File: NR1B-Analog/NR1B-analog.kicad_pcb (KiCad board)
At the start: 4 copper layers, 71.1 x 134.5 mm, 87 parts, among them J1 Conn_02x04_Odd_Even, J2 Conn_02x04_Odd_Even, J3 SWD, J8 UART, SW1 1-1571636-0, U1 DAC11001BPFBR, U10 LT3042MPMSE-PBF, U11 LDK320ADU120R, U12 20K, U13 OPA2189IDR, U14 DAC11001BPFBR, U2 ADR444ARZ, U3 OPA189IDGKT, U4 OPA2189IDR, U5 Pico, U6 OPA2189IDR, U7 LT3093EMSE-PBF, U8 20K, U9 10K, X1 NUCLEO144-ZIO

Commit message: BOM, fiducials
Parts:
- added FID1: Fiducial, Fiducial:Fiducial_0.5mm_Mask1.5mm, F.Cu at (50.8, 20.4)
- added FID2: Fiducial, Fiducial:Fiducial_0.5mm_Mask1.5mm, F.Cu at (118.1, 20.4)
- added FID3: Fiducial, Fiducial:Fiducial_0.5mm_Mask1.5mm, F.Cu at (117.1, 151.1)
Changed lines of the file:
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@@
       (net 70 "unconnected-(U8-Pad3)") (pinfunction "CW") (pintype "input+no_connect"))
+  )
+  (footprint "Fiducial:Fiducial_0.5mm_Mask1.5mm" (layer "F.Cu")
+    (at 50.77 20.35)
+    (descr "Circular Fiducial, 0.5mm bare copper, 1.5mm soldermask opening")
+    (tags "fiducial")
+    (property "Sheetfile" "NR1B-analog.kicad_sch")
+    (property "Sheetname" "")
+    (attr smd)
+    (fp_text reference "FID1" (at 2.73 -0.14) (layer "F.SilkS")
+      (effects (font (size 1 1) (thickness 0.15)))
+    )
+    (fp_text value "Fiducial" (at 0 1.7145) (layer "F.Fab")
+      (effects (font (size 1 1) (thickness 0.15)))
+    )
+    (fp_text user "${REFERENCE}" (at 0 0) (layer "F.Fab")
+      (effects (font (size 0.2 0.2) (thickness 0.04)))
+    )
+    (fp_circle (center 0 0) (end 1 0) (layer "F.CrtYd") (width 0.05) (fill none))
+    (fp_circle (center 0 0) (end 0.75 0) (layer "F.Fab") (width 0.1) (fill none))
+    (pad "" smd circle (at 0 0) (size 0.5 0.5) (layers "F.Cu" "F.Mask")
+      (solder_mask_margin 0.5) (clearance 0.5))
   )
   (footprint "Resistor_SMD:R_0603_1608Metric" (layer "F.Cu")
@@
     )
   )
+  (footprint "Fiducial:Fiducial_0.5mm_Mask1.5mm" (layer "F.Cu")
+    (at 117.1 151.11)
+    (descr "Circular Fiducial, 0.5mm bare copper, 1.5mm soldermask opening")
+    (tags "fiducial")
+    (property "Sheetfile" "NR1B-analog.kicad_sch")
+    (property "Sheetname" "")
+    (attr smd)
+    (fp_text reference "FID3" (at 0 -1.7145) (layer "F.SilkS")
+      (effects (font (size 1 1) (thickness 0.15)))
+    )
+    (fp_text value "Fiducial" (at 0 1.7145) (layer "F.Fab")
+      (effects (font (size 1 1) (thickness 0.15)))
+    )
+    (fp_text user "${REFERENCE}" (at 0 0) (layer "F.Fab")
+      (effects (font (size 0.2 0.2) (thickness 0.04)))
+    )
+    (fp_circle (center 0 0) (end 1 0) (layer "F.CrtYd") (width 0.05) (fill none))
+    (fp_circle (center 0 0) (end 0.75 0) (layer "F.Fab") (width 0.1) (fill none))
+    (pad "" smd circle (at 0 0) (size 0.5 0.5) (layers "F.Cu" "F.Mask")
+      (solder_mask_margin 0.5) (clearance 0.5))
+  )
   (footprint "Resistor_SMD:R_0603_1608Metric" (layer "F.Cu")
     (at 90.73 51.32 -90)
@@
     )
   )
+  (footprint "Fiducial:Fiducial_0.5mm_Mask1.5mm" (layer "F.Cu")
+    (at 118.08 20.35)
+    (descr "Circular Fiducial, 0.5mm bare copper, 1.5mm soldermask opening")
+    (tags "fiducial")
+    (property "Sheetfile" "NR1B-analog.kicad_sch")
+    (property "Sheetname" "")
+    (attr smd)
+    (fp_text reference "FID2" (at -2.98 0.12) (layer "F.SilkS")
+      (effects (font (size 1 1) (thickness 0.15)))
+    )
+    (fp_text value "Fiducial" (at 0 1.7145) (layer "F.Fab")
+      (effects (font (size 1 1) (thickness 0.15)))
+    )
+    (fp_text user "${REFERENCE}" (at 0 0) (layer "F.Fab")
+      (effects (font (size 0.2 0.2) (thickness 0.04)))
+    )
+    (fp_circle (center 0 0) (end 1 0) (layer "F.CrtYd") (width 0.05) (fill none))
+    (fp_circle (center 0 0) (end 0.75 0) (layer "F.Fab") (width 0.1) (fill none))
+    (pad "" smd circle (at 0 0) (size 0.5 0.5) (layers "F.Cu" "F.Mask")
+      (solder_mask_margin 0.5) (clearance 0.5))
+  )
   (footprint "TestPoint:TestPoint_Bridge_Pitch2.0mm_Drill0.7mm" (layer "F.Cu")

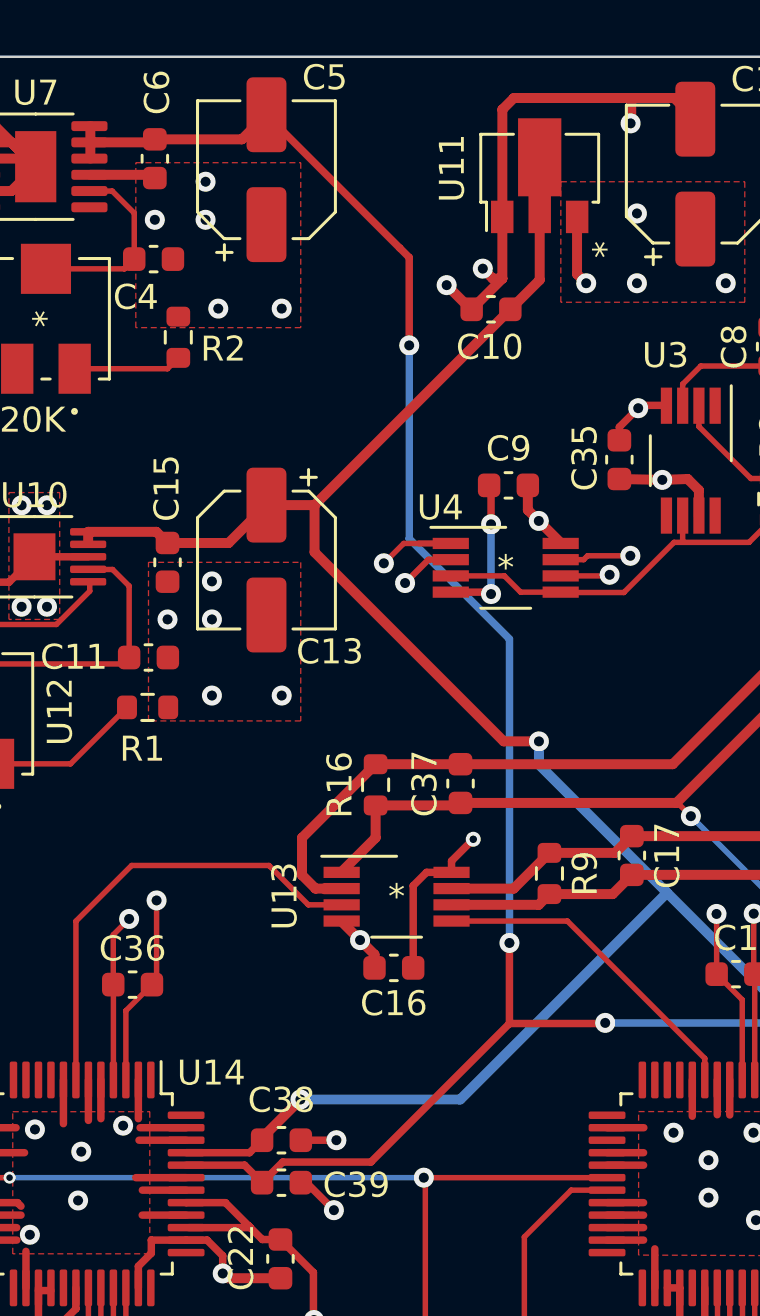
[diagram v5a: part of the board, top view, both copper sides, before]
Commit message: Cap footprints adjusted for size constraints
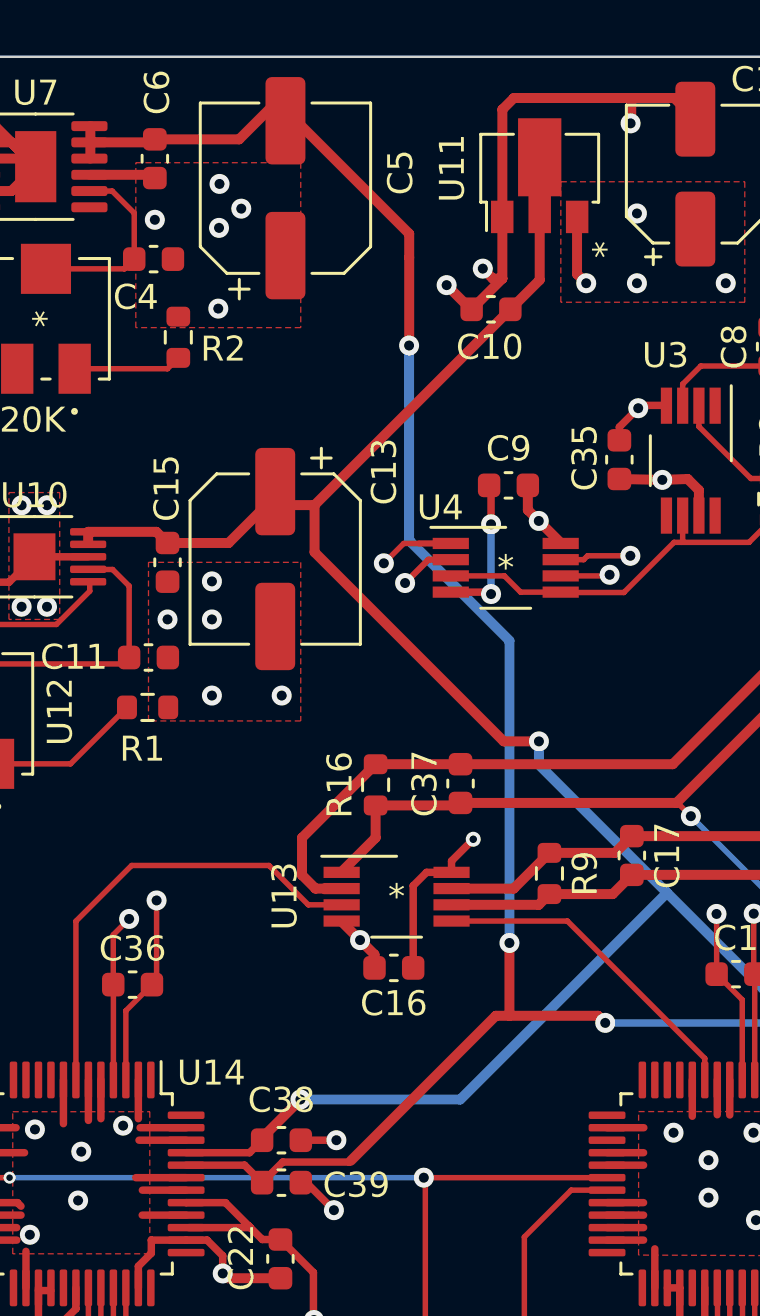
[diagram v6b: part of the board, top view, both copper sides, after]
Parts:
- C13, C5: footprint Capacitor_SMD:CP_Elec_5x5.3 -> Capacitor_SMD:CP_Elec_6.3x5.8
- R1: value 130k -> 130K
- moved C5 1.06 mm to (80.2, 23.9)
- moved C13 0.35 mm to (79.8, 38.7)
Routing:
- net -14Vreg: track 87.2 -> 88.1 mm

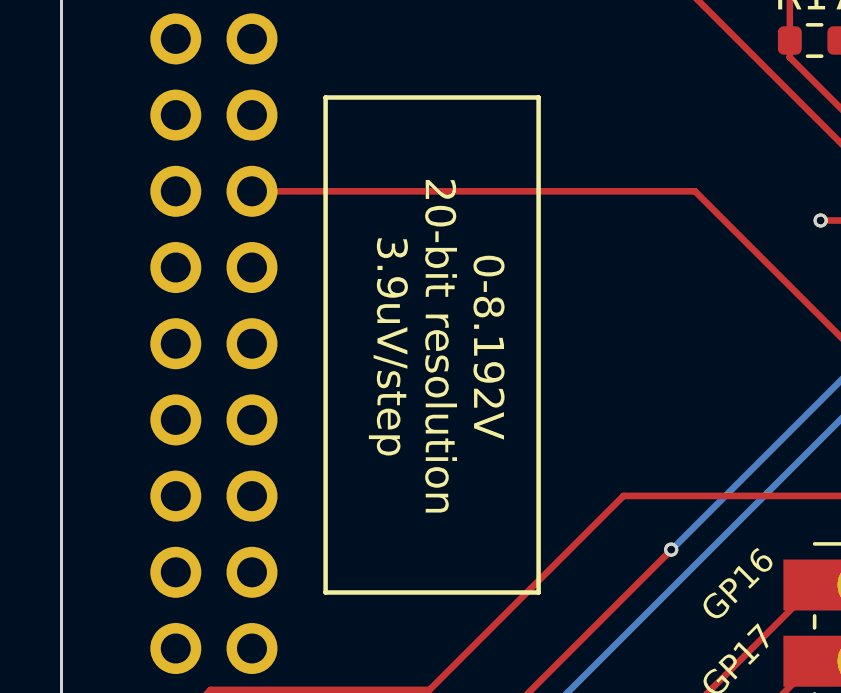
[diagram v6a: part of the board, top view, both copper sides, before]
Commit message: Updated silkscreen
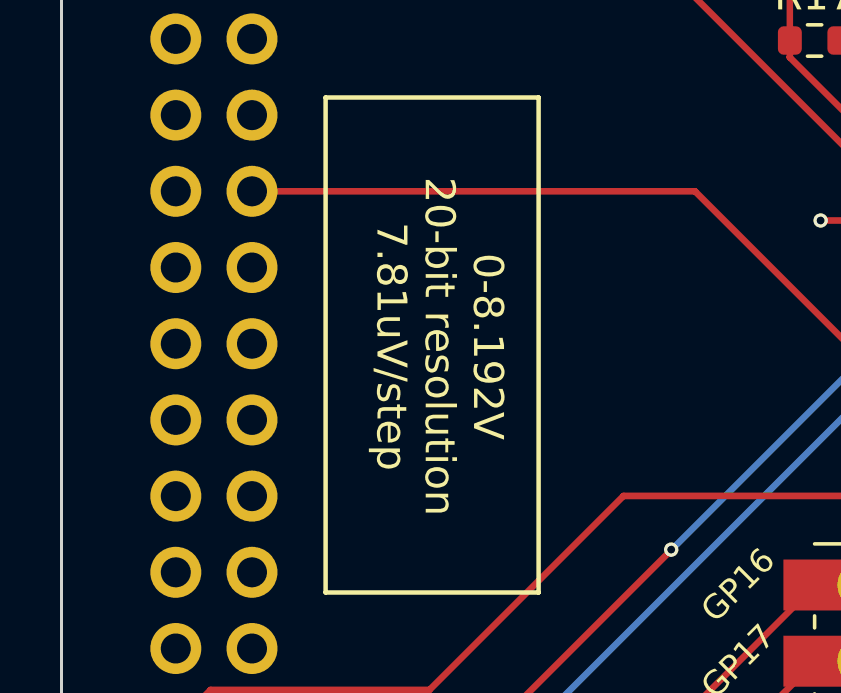
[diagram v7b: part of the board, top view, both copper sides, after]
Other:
- board text added: "0-8.192V 20-bit resolution 7.81uV/step"
- board text removed: "0-8.192V 20-bit resolution 3.9uV/step"
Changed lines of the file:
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@@
     (effects (font (size 1 1) (thickness 0.15)))
   )
-  (gr_text "0-8.192V\n20-bit resolution\n3.9uV/step\n" (at 61.6 94.2 270) (layer "F.SilkS")
+  (gr_text "0-8.192V\n20-bit resolution\n7.81uV/step\n" (at 61.6 94.2 270) (layer "F.SilkS")
     (effects (font (size 1 1) (thickness 0.15)))
   )

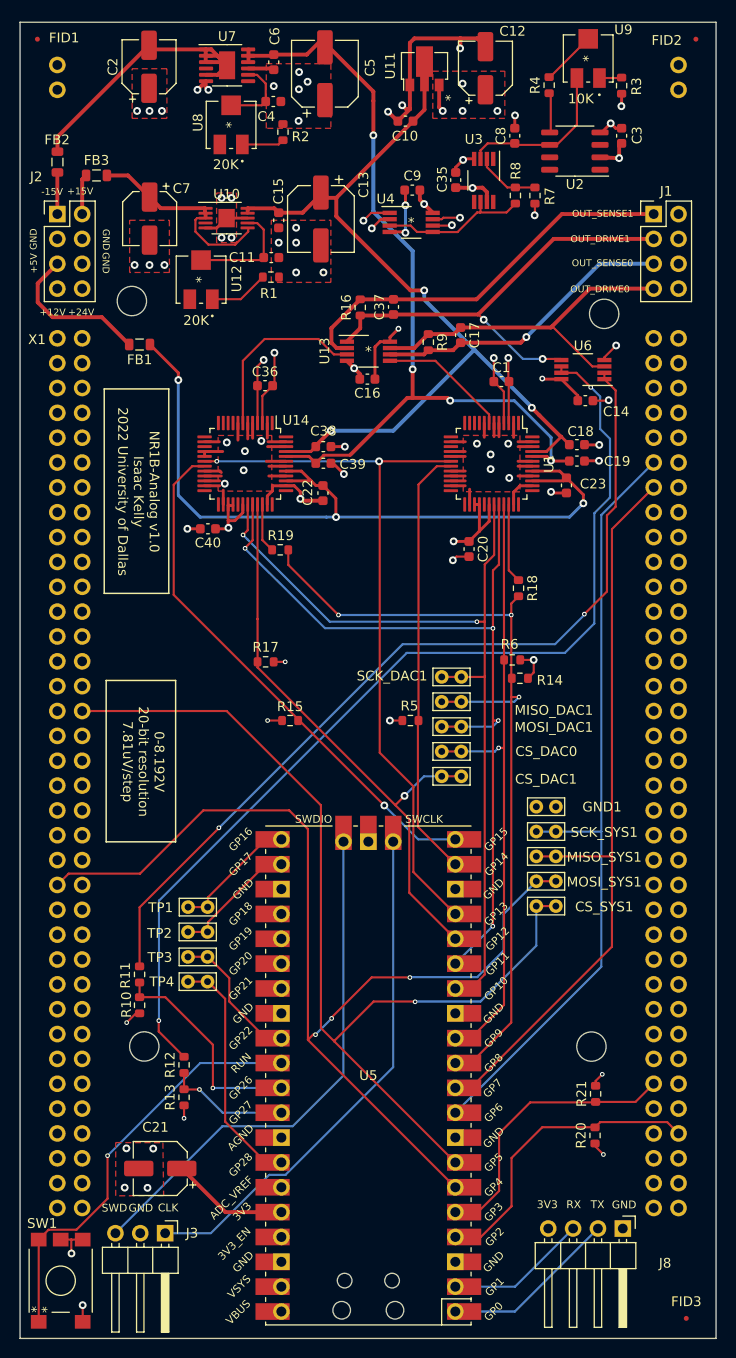
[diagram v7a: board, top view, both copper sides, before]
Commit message: Changed footprints, re-routed
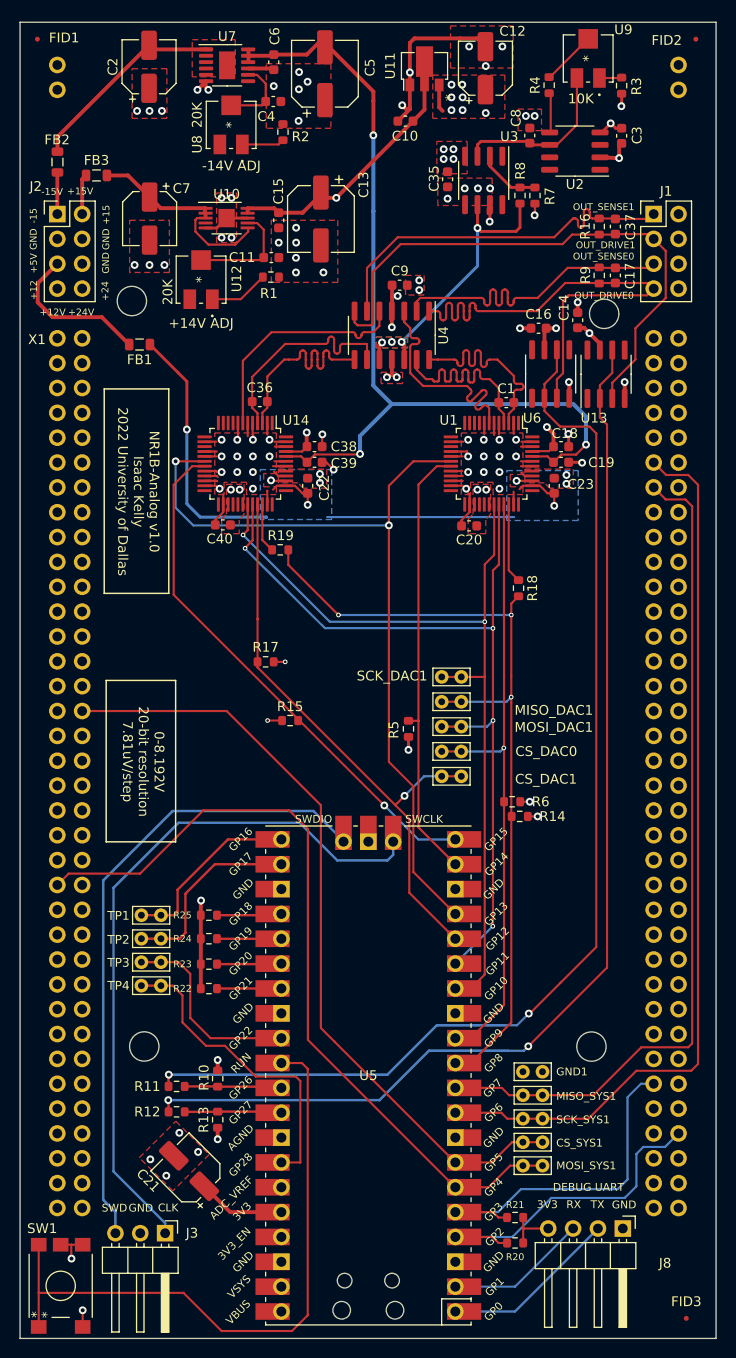
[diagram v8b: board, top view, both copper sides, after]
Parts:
- added R22: 10K, Resistor_SMD:R_0603_1608Metric, F.Cu at (68.3, 117.4)
- added R23: 10K, Resistor_SMD:R_0603_1608Metric, F.Cu at (68.3, 114.9)
- added R24: 10K, Resistor_SMD:R_0603_1608Metric, F.Cu at (68.3, 112.3)
- added R25: 10K, Resistor_SMD:R_0603_1608Metric, F.Cu at (68.3, 109.9)
- U13, U6: value OPA2189IDR -> OPA189ID; footprint Package_SO:VSSOP-8_3.0x3.0mm_P0.65mm -> Package_SO:SOIC-8_3.9x4.9mm_P1.27mm
- U3: footprint Package_SO:VSSOP-8_3.0x3.0mm_P0.65mm -> Package_SO:SOIC-8_3.9x4.9mm_P1.27mm
- U4: value OPA2189IDR -> OPA4182; footprint Package_SO:VSSOP-8_3.0x3.0mm_P0.65mm -> Package_SO:SOIC-14_3.9x8.7mm_P1.27mm
- moved SCK_SYS1 29.4 mm to (100.4, 130.7)
- moved MOSI_SYS1 29.1 mm to (100.4, 135.5)
- moved GND1 27.1 mm to (100.4, 125.9)
- moved R16 25.8 mm to (108.2, 39.5)
- moved MISO_SYS1 24.5 mm to (100.4, 128.3)
- moved U13 24.4 mm to (108.9, 54.6), turned to 90 degrees
- moved CS_SYS1 24.2 mm to (100.4, 133.1)
- moved C37 24.1 mm to (109.8, 39.5)
- moved R9 18.8 mm to (108.2, 44.5), turned to 90 degrees
- moved C16 18.3 mm to (102.0, 49.9), turned to 0 degrees
- moved C17 17.0 mm to (109.8, 44.5), turned to 90 degrees
- moved R21 15.1 mm to (99.6, 140.8), turned to 0 degrees
- moved R6 14.5 mm to (99.3, 98.3)
- moved R14 14.1 mm to (100.1, 99.8)
- moved R20 13.7 mm to (99.6, 143.4), turned to 180 degrees
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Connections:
- C14 pad 1: +12Vref -> GND
- C14 pad 2: GND -> +12Vref
- C16 pad 1: +12Vref -> GND
- C16 pad 2: GND -> +12Vref
- C9 pad 1: +12Vref -> GND
- C9 pad 2: GND -> +12Vref
- U13 pad 1: OUT_DRIVE1 -> unconnected-(U13-Pad1)
- U13 pad 2: OUT_SENSE1 -> Net-(R12-Pad2)
- U13 pad 3: Net-(U13-Pad3) -> OUT_DRIVE1
- U13 pad 5: Net-(U1-Pad7) -> unconnected-(U13-Pad5)
- U13 pad 6: OUT_SENSE0 -> Net-(R12-Pad2)
- U13 pad 7: OUT_DRIVE0 -> +12Vref
- U13 pad 8: +12Vref -> unconnected-(U13-Pad8)
- U14 pad 7: Net-(U13-Pad3) -> Net-(U14-Pad7)
- U4 pad 1: Net-(C36-Pad2) -> OUT_DRIVE0
- U4 pad 2: Net-(C36-Pad1) -> OUT_SENSE0
- U4 pad 3: REF_OUT -> Net-(U1-Pad7)
- U4 pad 4: GND -> +12Vref
- U4 pad 5: REF_OUT -> Net-(U14-Pad7)
- U4 pad 6: Net-(C1-Pad1) -> OUT_SENSE1
- U4 pad 7: Net-(C1-Pad2) -> OUT_DRIVE1
- U4 pad 8: +12Vref -> Net-(C36-Pad2)
- U5 pad 24: GND -> Net-(R25-Pad1)
- U5 pad 25: GND -> Net-(R24-Pad1)
- U5 pad 26: GND -> Net-(R23-Pad1)
- U5 pad 27: GND -> Net-(R22-Pad1)
- U6 pad 1: Net-(R11-Pad1) -> unconnected-(U6-Pad1)
- U6 pad 5: OUT_DRIVE1 -> unconnected-(U6-Pad5)
- U6 pad 6: Net-(R12-Pad2) -> Net-(R11-Pad1)
- U6 pad 7: Net-(R12-Pad2) -> +12Vref
- U6 pad 8: +12Vref -> unconnected-(U6-Pad8)
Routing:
- net +5V: track 81.0 -> 48.8 mm, vias 3 -> 7
- net Net-(R11-Pad1): track 90.3 -> 115.8 mm
- net /Interconnect/MOSI: track 106.6 -> 82.3 mm, vias 3 -> 0
- net Net-(U14-Pad7): track 0.00 -> 24.0 mm
- net Net-(SW1-Pad1): track 43.3 -> 66.3 mm, vias 1 -> 0
- net /Interconnect/NSS: track 101.4 -> 80.4 mm, vias 1 -> 0
- net Net-(J3-Pad1): track 53.4 -> 72.1 mm
- net Net-(U13-Pad3): track 18.6 -> 0.00 mm
- net +3V3: track 47.8 -> 29.4 mm, vias 8 -> 9
- net OUT_DRIVE0: track 36.5 -> 53.1 mm
- net GND: track 135.2 -> 122.1 mm, vias 61 -> 86
- net REF_OUT: track 15.4 -> 28.1 mm, vias 0 -> 4
- net /MCU/DAC0_READ: track 22.4 -> 9.95 mm, vias 1 -> 0
- net Net-(R12-Pad2): track 103.2 -> 115.6 mm
- net Net-(J3-Pad3): track 53.9 -> 65.4 mm
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- added copper zone on F.Cu, net +3V3
- added copper zone on B.Cu, net +5V
- added copper zone on F.Cu, net +5V
- added copper zone on F.Cu, net -15Vreg
- added copper zone on B.Cu, net REF_OUT
- added copper zone on F.Cu, net REF_OUT
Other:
- board text added: "+12"
- board text added: "+14V ADJ"
- board text added: "+15"
- board text added: "+24"
- board text added: "-14V ADJ"
- board text added: "-15"
- board text added: "DEBUG UART"
